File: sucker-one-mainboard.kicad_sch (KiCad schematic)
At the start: 111 parts, among them J1 JST NC Valve, J10 JST Motor, J11 Conn_02x04_Odd_Even, J12 TYPE-C-31-M-12, J2 JST NO Valve, J3 6P4C, J4 JST 3 Way Valve, J5 Jack-DC, J6 Phoenix Contact 1733570, J7 QWIIC I2C, J8 SPI, J9 52271-1079, Q1 BSS138, Q2 BSS138, Q3 BSS138, Q4 STN4NF20L, Q5 FDN304PZ, SW1 BOOT0, SW2 RST, U1 LD1117S33TR, U2 LM2596SX-5.0/NOPB, U3 LM358D, U4 STM32F401CDUx, Y1 8MHz(16pf)

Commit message: STM32 version
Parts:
- added Q6: STN4NF20L, STN4NF20L:SOT223, symbol STN4NF20L:STN4NF20L
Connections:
- new net: Q6.2, Q6.T
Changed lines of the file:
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@@
     (pin "4")
+  )
+  (symbol (lib_id "STN4NF20L:STN4NF20L") (at 254.635 77.47 0) (unit 1)
+    (in_bom yes) (on_board yes)
+    (property "Reference" "Q6" (id 0) (at 257.81 76.2 0)
+      (effects (font (size 1.27 1.27)) (justify left))
+    )
+    (property "Value" "STN4NF20L" (id 1) (at 257.81 78.74 0)
+      (effects (font (size 1.27 1.27)) (justify left))
+    )
+    (property "Footprint" "STN4NF20L:SOT223" (id 2) (at 254.635 77.47 0)
+      (effects (font (size 1.27 1.27)) (justify left bottom) hide)
+    )
+    (property "Datasheet" "" (id 3) (at 254.635 77.47 0)
+      (effects (font (size 1.27 1.27)) (justify left bottom) hide)
+    )
+    (property "PARTNO" "497-10779-1-ND" (id 4) (at 254.635 77.47 0)
+      (effects (font (size 1.27 1.27)) (justify left bottom) hide)
+    )
+    (pin "3")
+    (pin "1")
+    (pin "2")
+    (pin "T")
   )
   (symbol (lib_id "Connector:Jack-DC") (at 91.44 130.81 0) (unit 1)
@@
       (reference "Q5") (unit 1) (value "FDN304PZ") (footprint "FDN304PZ:ON_Semi-FDN304PZ-0")
     )
+    (path "/6743ab98-b769-4bae-8779-5add1a10e4f3"
+      (reference "Q6") (unit 1) (value "STN4NF20L") (footprint "STN4NF20L:SOT223")
+    )
     (path "/a7126a39-1007-41f3-a3ae-2fffa13ffc7e"

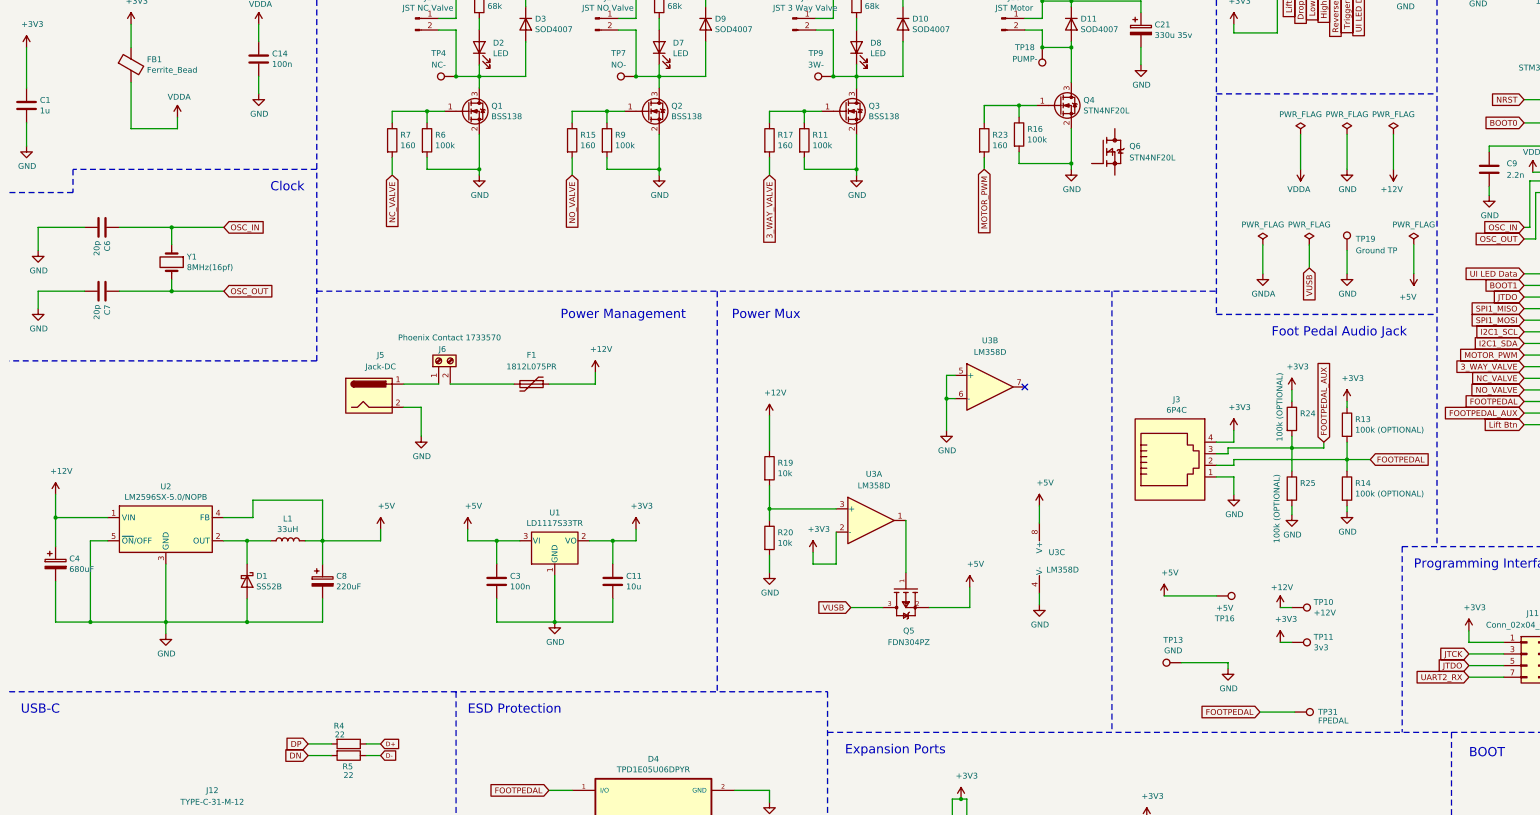
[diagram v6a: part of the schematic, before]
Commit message: Change DC-DC 5V converter to TPS561201DDCR
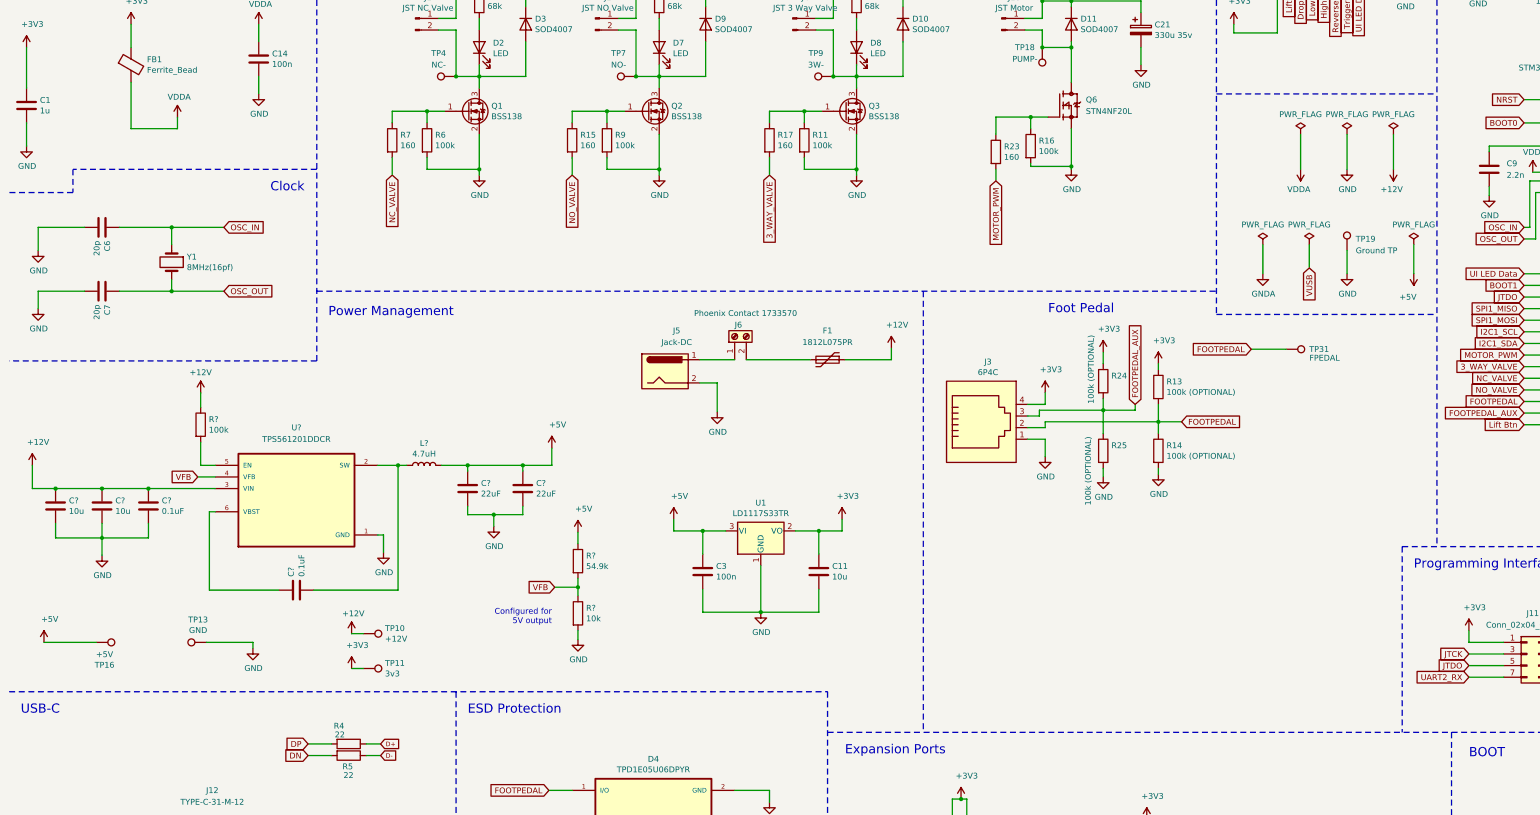
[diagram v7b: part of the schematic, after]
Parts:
- removed C4: 680uF, Capacitor_SMD:CP_Elec_10x10.5, symbol Heizrelaissteuerung-rescue:CP-Device
- removed C8: 220uF, Capacitor_Tantalum_SMD:CP_EIA-6032-28_Kemet-C_Pad2.25x2.35mm_HandSolder, symbol Heizrelaissteuerung-rescue:CP-Device
- removed D1: SS52B, Diode_SMD:D_SMB, symbol Diode:1N5822
- removed L1: 33uH, Inductor_SMD:L_Bourns_SRN6045TA, symbol Device:L
- removed Q4: STN4NF20L, Package_TO_SOT_SMD:SOT-223, symbol Transistor_FET:BSS138
- removed Q5: FDN304PZ, FDN304PZ:ON_Semi-FDN304PZ-0, symbol FDN304PZ:FDN304PZ
- removed R19, R20: 10k, Resistor_SMD:R_0603_1608Metric_Pad0.98x0.95mm_HandSolder, symbol Device:R
- removed U2: LM2596SX-5.0/NOPB, Package_TO_SOT_SMD:TO-263-5_TabPin3, symbol Regulator_Switching:LM2596S-5
- removed U3: LM358D, LM358D:SOIC127P599X175-8N, symbol Amplifier_Operational:LM358
- added C? (x2): 10u, Capacitor_SMD:C_0603_1608Metric_Pad1.08x0.95mm_HandSolder, symbol Device:C
- added C? (x2): 0.1uF, Capacitor_SMD:C_0603_1608Metric_Pad1.08x0.95mm_HandSolder, symbol Device:C
- added C? (x2): 22uF, Capacitor_SMD:C_0603_1608Metric_Pad1.08x0.95mm_HandSolder, symbol Device:C
- added L?: 4.7uH, Inductor_SMD:L_Bourns_SRN6045TA, symbol Device:L
- added R?: 100k, Resistor_SMD:R_0603_1608Metric_Pad0.98x0.95mm_HandSolder, symbol Device:R
- added R?: 10k, Resistor_SMD:R_0603_1608Metric_Pad0.98x0.95mm_HandSolder, symbol Device:R
- added R?: 54.9k, Resistor_SMD:R_0603_1608Metric_Pad0.98x0.95mm_HandSolder, symbol Device:R
- added U?: TPS561201DDCR, SOT95P280X110-6N, symbol TPS561201DDCR:TPS561201DDCR
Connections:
- net +12V: now also C?.1, C?.1, C?.1, R?.1, U?.3 (VIN)
- net +5V: now also C?.1, C?.1, L?.2, R?.1
- net GND: now also Q6.3, C?.2, C?.2, C?.2, C?.2, C?.2, R?.2, U?.1 (GND)
- net at R16.1, R23.1: now also Q6.1
- net at D11.2 (A), J10.2 (Pin_2), TP18.1: now also Q6.2, Q6.T
- new net: C?.2, L?.1, U?.2 (SW)
- new net: C?.1, U?.6 (VBST)
- new net: R?.2, U?.5 (EN)
- new net VFB: R?.1, R?.2, U?.4 (VFB)
- no-connect marks 9 -> 8
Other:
- note added: "Configured for 5V output"
- note added: "Foot Pedal"
- note removed: "Foot Pedal Audio Jack"
- note removed: "Power Mux"
- moved on the sheet: C11, C3, F1, J3, J5, J6, Q6, R13, R14, R16, R23, R24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

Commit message: Change from STM32 to RP2040
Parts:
- removed C19: 100n, Capacitor_SMD:C_0603_1608Metric_Pad1.08x0.95mm_HandSolder, symbol Device:C
- removed C9: 2.2n, Capacitor_SMD:C_0603_1608Metric_Pad1.08x0.95mm_HandSolder, symbol Device:C
- removed R18: 100k, Resistor_SMD:R_0603_1608Metric_Pad0.98x0.95mm_HandSolder, symbol Device:R
- removed R26: 0 (OPTIONAL), Resistor_SMD:R_0603_1608Metric_Pad0.98x0.95mm_HandSolder, symbol Device:R
- removed R27: 10k, Resistor_SMD:R_0603_1608Metric_Pad0.98x0.95mm_HandSolder, symbol Device:R
- removed R28, R29: 0, Resistor_SMD:R_0603_1608Metric_Pad0.98x0.95mm_HandSolder, symbol Device:R
- removed SW1: BOOT0, Button_Switch_SMD:SW_SPST_B3U-1000P, symbol Switch:SW_Push
- removed SW2: RST, Button_Switch_SMD:SW_SPST_B3U-1000P, symbol Switch:SW_Push
- removed TP20: BOOT1, TestPoint:TestPoint_Pad_D2.0mm, symbol Connector:TestPoint
- removed TP30: BOOT0, TestPoint:TestPoint_Pad_D2.0mm, symbol Connector:TestPoint
- removed TP5: NRST, TestPoint:TestPoint_Pad_D2.0mm, symbol Connector:TestPoint
- removed U4: STM32F401CDUx, Package_DFN_QFN:QFN-48-1EP_7x7mm_P0.5mm_EP5.6x5.6mm, symbol MCU_ST_STM32F4:STM32F401CDUx
- added C? (x10): 100n, Capacitor_SMD:C_0603_1608Metric_Pad1.08x0.95mm_HandSolder, symbol Device:C
- added C? (x2): 1u, Capacitor_SMD:C_0603_1608Metric_Pad1.08x0.95mm_HandSolder, symbol Device:C
- added R?: 10k (OPTIONAL), Resistor_SMD:R_0603_1608Metric_Pad0.98x0.95mm_HandSolder, symbol Device:R
- added R? (x2): 1k, Resistor_SMD:R_0603_1608Metric_Pad0.98x0.95mm_HandSolder, symbol Device:R
- added SW?: BOOTSEL, symbol Switch:SW_Push
- added TP?: SWCLK, TestPoint:TestPoint_Pad_D2.0mm, symbol Connector:TestPoint
- added TP?: RUN, TestPoint:TestPoint_Pad_D2.0mm, symbol Connector:TestPoint
- added U?: W25Q128JVS, Package_SO:SOIC-8_5.23x5.23mm_P1.27mm, symbol Memory_Flash:W25Q128JVS
- added U?: RP2040, RP2040_minimal:RP2040-QFN-56, symbol RP2040:RP2040
- C6, C7: value 20p -> 27p
- R4, R5: value 22 -> 27.4
- TP14: value I2C1 SCL -> I2C0 SCL
- TP15: value I2C1 SDA -> I2C0 SDA
- TP22: value JTCK -> UARTRX
- TP23: value JTMS -> UARTTX
- TP24: value JTDO -> SWDIO
- TP25: value SPI1 CS -> SPI0 CS
- TP26: value SPI1 CLK -> SPI0 CLK
- TP27: value SPI1 MISO -> SPI0 MISO
- TP28: value SPI1 MOSI -> SPI0 MOSI
- Y1: value 8MHz(16pf) -> ABLS-12.000MHZ-B4-T; footprint Crystal:Crystal_SMD_5032-2Pin_5.0x3.2mm -> (none)
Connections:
- net UART2_RX is gone; now on net GND: J11.7 (Pin_7)
- net UART2_TX is gone; now on net GND: J11.8 (Pin_8)
- net +3V3: now also C?.1, C?.2, C?.2, C?.2, C?.2, C?.2, C?.2, C?.2, C?.2, R?.1, U?.1 (IOVDD), U?.10 (IOVDD), U?.22 (IOVDD), U?.33 (IOVDD), U?.42 (IOVDD), U?.43 (ADC_AVDD), U?.44 (VREG_IN), U?.48 (USB_VDD), U?.49 (IOVDD), U?.8 (VCC); no longer J11.1 (Pin_1)
- net 3_WAY_VALVE: now also U?.6 (GPIO4)
- net D+: now also U?.47 (USB_DP)
- net D-: now also U?.46 (USB_DM)
- net FOOTPEDAL: now also U?.8 (GPIO6)
- net FOOTPEDAL_AUX: now also U?.9 (GPIO7)
- net GND: now also C?.1, C?.1, C?.1, C?.1, C?.1, C?.1, C?.1, C?.1, C?.1, C?.1, C?.2, C?.2, SW?.2, U?.19 (TESTEN), U?.4 (GND), U?.57 (GND); no longer J11.2 (Pin_2)
- net High Btn: now also U?.13 (GPIO10)
- net Lift Btn: now also U?.11 (GPIO8)
- net Low Btn: now also U?.14 (GPIO11)
- net MOTOR_PWM: now also U?.7 (GPIO5)
- net NC_VALVE: now also U?.5 (GPIO3)
- net NO_VALVE: now also U?.4 (GPIO2)
- net OSC_IN: now also U?.20 (XIN)
- net OSC_OUT: now also R?.1, U?.21 (XOUT); no longer C7.1, Y1.2
- net Reverse Btn: now also U?.15 (GPIO12)
- net SPI1_CS: now also U?.32 (GPIO21); no longer J8.2 (Pin_2), TP25.1
- net Trigger Btn: now also U?.16 (GPIO13)
- net UI LED Data: now also U?.17 (GPIO14)
- net VUSB: no longer J12.A4B9 (VBUS), J12.B4A9 (VBUS)
- net BOOT0 renamed Drop Btn
- net Drop Btn: now also U?.12 (GPIO9)
- net I2C1_SCL renamed I2C0_SCL
- net I2C0_SCL: now also U?.28 (GPIO17)
- net I2C1_SDA renamed I2C0_SDA
- net I2C0_SDA: now also U?.27 (GPIO16)
- net JTCK renamed UART0_RX
- net UART0_RX: now also J11.1 (Pin_1), U?.3 (GPIO1); no longer J11.3 (Pin_3)
- net JTDO renamed SWDIO
- net SWDIO: now also U?.25 (SWD)
- net JTMS: no longer names the net of J11.4 (Pin_4)
- net JTMS: no longer TP23.1
- net NRST renamed SWCLK
- net SWCLK: now also TP?.1, U?.24 (SWCLK)
- net SPI1_CLK renamed SPI0_CLK
- net SPI0_CLK: now also U?.29 (GPIO18)
- net SPI1_MISO renamed SPI0_MISO
- net SPI0_MISO: now also U?.31 (GPIO20)
- net SPI1_MOSI renamed SPI0_MOSI
- net SPI0_MOSI: now also U?.30 (GPIO19)
- new net: C7.1, R?.2, Y1.2
- new net: R?.2, SW?.1
- new net: TP?.1, U?.26 (RUN)
- new net: J12.A4B9 (VBUS), J12.B4A9 (VBUS)
- new net +1V1: C?.1, C?.2, U?.23 (DVDD), U?.45 (VREG_VOUT), U?.50 (DVDD)
- new net QSPI_SCLK: U?.52 (QSPI_SCLK), U?.6 (CLK)
- new net QSPI_SD0: U?.5 (DI(IO0)), U?.53 (QSPI_SD0)
- new net QSPI_SD1: U?.2 (DO(IO1)), U?.55 (QSPI_SD1)
- new net QSPI_SD2: U?.3 (IO2), U?.54 (QSPI_SD2)
- new net QSPI_SD3: U?.51 (QSPI_SD3), U?.7 (IO3)
- new net QSPI_SS: R?.1, R?.2, U?.1 (~CS), U?.56 (QSPI_SS)
- new net SPI0_CS: J8.2 (Pin_2), TP25.1
- new net UART0_TX: J11.3 (Pin_3), TP23.1, U?.2 (GPIO0)
- no-connect marks 8 -> 14
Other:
- note added: "FLASH"
- note added: "Place as close to pin 44 as possible"
- note added: "Place as close to pin 45 as possible"
- note added: "Place close to the RP2040"
- note added: "RP2040"
- note added: "UART / SWD"
- note removed: "BOOT"
- note removed: "BOOT0 to GND will always boot into flash memory"
- note removed: "MCU"
- note removed: "Programming Interface"
- moved on the sheet: D12, D4, D5, D6, J11, J3, J7, J8, J9, R13, R14, R21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
